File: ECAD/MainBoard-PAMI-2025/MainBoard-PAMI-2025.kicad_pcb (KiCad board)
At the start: 2 copper layers, 80 x 80 mm, 53 parts, among them J1 Sensor_Center, J10 Serial, J11 Con_Batt, J13 OLED, J2 USB_B, J3 Sensor_RIGHT, J4 Servo, J5 Sensor_LEFT, J6 Servo, J7 LeftMotor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

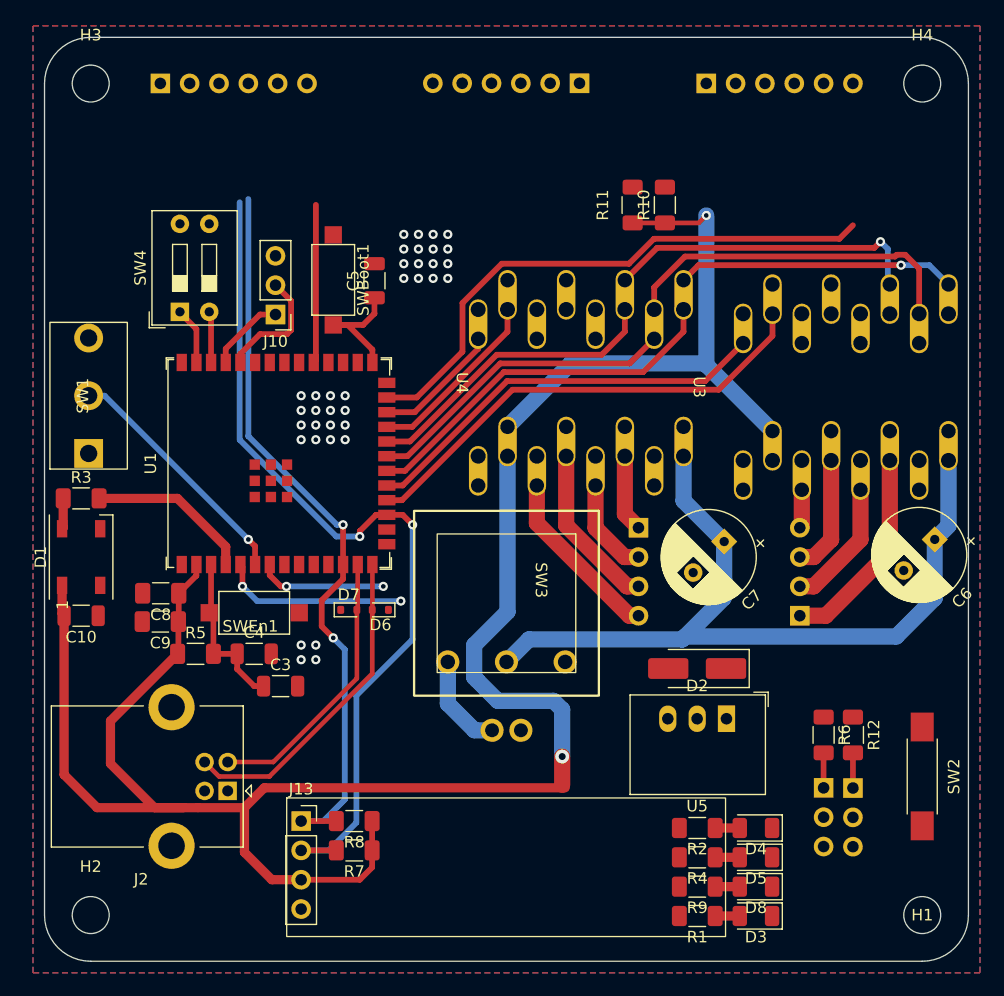
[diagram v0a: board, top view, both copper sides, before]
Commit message: Update Live 206
Update Battery
Add Recom 5V
Add ASM1117
Add capacitor
Change sensor header
Move components
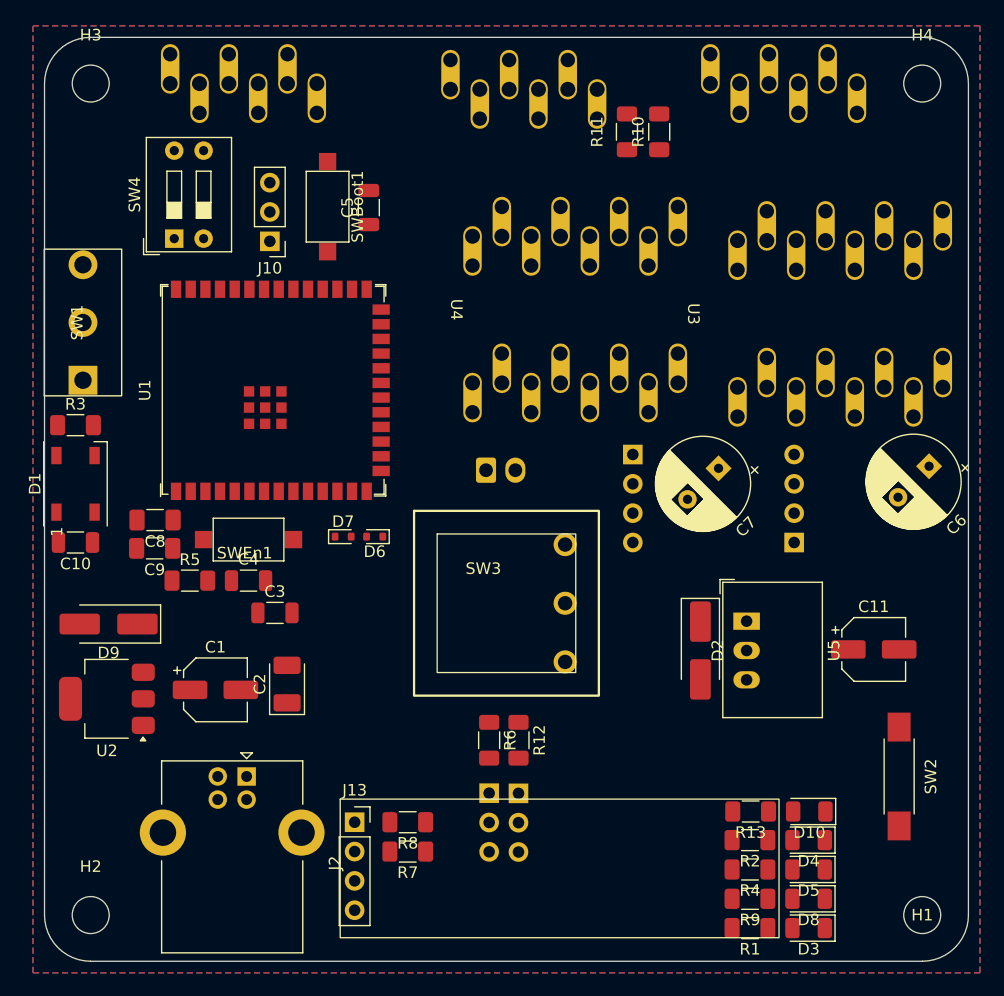
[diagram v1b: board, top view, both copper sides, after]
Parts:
- added C1: 10uF, Capacitor_SMD:CP_Elec_5x5.4, F.Cu at (94.8, 121.5)
- added C11: 22uF, Capacitor_SMD:CP_Elec_5x5.4, F.Cu at (151.8, 118.0)
- added C2: 22uF, Capacitor_Tantalum_SMD:CP_EIA-3528-12_Kemet-T_Pad1.50x2.35mm_HandSolder, F.Cu at (101.0, 121.0)
- added D10: Green, LED_SMD:LED_1206_3216Metric, F.Cu at (146.2, 132.0)
- added D9: D_Small, Diode_SMD:D_SMA_Handsoldering, F.Cu at (85.5, 115.8)
- added R13: 1K, Resistor_SMD:R_1206_3216Metric_Pad1.30x1.75mm_HandSolder, F.Cu at (141.1, 132.0)
- added U2: AMS1117-3.3, Package_TO_SOT_SMD:SOT-223-3_TabPin2, F.Cu at (85.4, 122.3)
- J1, J3, J5: footprint Connector_PinSocket_2.54mm:PinSocket_1x06_P2.54mm_Vertical -> PAMI-2025:VL53 Bottom Entry Version
- J11: footprint PAMI-2025:LP-e6 Batterie -> Connector_Molex:Molex_KK-254_AE-6410-02A_1x02_P2.54mm_Vertical
- U5: value R-78E3.3-1.0 -> R-78E5.0-1.0
- moved J4 29.0 mm to (118.5, 130.4)
- moved R6 29.0 mm to (118.5, 125.9)
- moved J6 29.0 mm to (121.0, 130.5)
- moved R12 29.0 mm to (121.0, 125.9)
- moved J11 22.6 mm to (118.2, 102.5), turned to 0 degrees
- moved U5 8.62 mm to (140.8, 115.6), turned to -90 degrees
- moved J5 7.20 mm to (97.2, 69.0)
- moved J3 6.70 mm to (144.0, 69.0)
- moved C4 6.36 mm to (97.7, 112.0)
- moved C6 6.36 mm to (156.6, 102.1)
- moved C7 6.36 mm to (138.4, 102.3)
- moved D6 6.36 mm to (108.6, 108.2)
- moved D7 6.36 mm to (105.9, 108.2)
- moved J8 6.36 mm to (144.9, 108.7)
- moved U3 6.36 mm to (148.9, 88.9)
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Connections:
- C6 pad 1: +5VP -> +9V
- C7 pad 1: +5VP -> +9V
- D2 pad 1: +5VP -> +9V
- D2 pad 2: +3.3V -> +5VP
- J4 pad 2: +3.3V -> +5VP
- J6 pad 2: +3.3V -> +5VP
- R2 pad 2: +5VP -> +9V
- SW3 pad 2: +5VP -> +9V
- U3 pad 16: +5VP -> +9V
- U4 pad 16: +5VP -> +9V
- U5 pad 1: +5VP -> +9V
- U5 pad 3: +3.3V -> +5VP
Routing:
- net +3.3V: track 193.7 -> 0.00 mm, vias 2 -> 0
- net SCL: track 77.1 -> 0.00 mm, vias 2 -> 0
- net +5VP: track 70.6 -> 0.00 mm
- net SDA: track 64.9 -> 0.00 mm, vias 2 -> 0
- net LeftMS1: track 57.8 -> 0.00 mm
- net EnDriver: track 56.8 -> 0.00 mm, vias 1 -> 0
- net LeftMS2: track 54.0 -> 0.00 mm, vias 1 -> 0
- net XSHUT_RIGHT: track 49.0 -> 0.00 mm
- net RightStep: track 41.2 -> 0.00 mm
- net RightDir: track 36.0 -> 0.00 mm
- net /D+: track 28.2 -> 0.00 mm
- net /D-: track 24.1 -> 0.00 mm
- net Color_Team: track 21.4 -> 0.00 mm, vias 1 -> 0
- net Net-(J8-Pin_1): track 18.0 -> 0.00 mm
- net Tirette: track 16.2 -> 0.00 mm, vias 2 -> 0
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
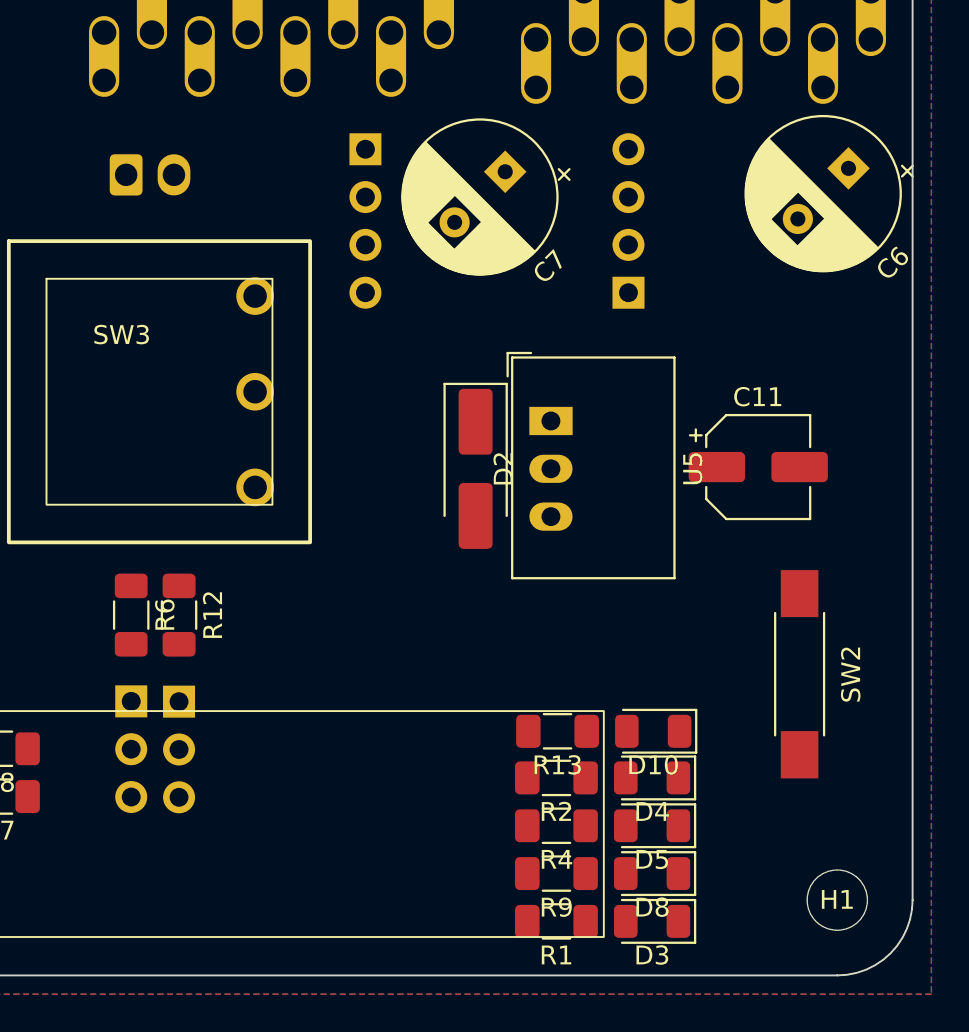
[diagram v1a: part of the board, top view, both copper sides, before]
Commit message: Add buzzer
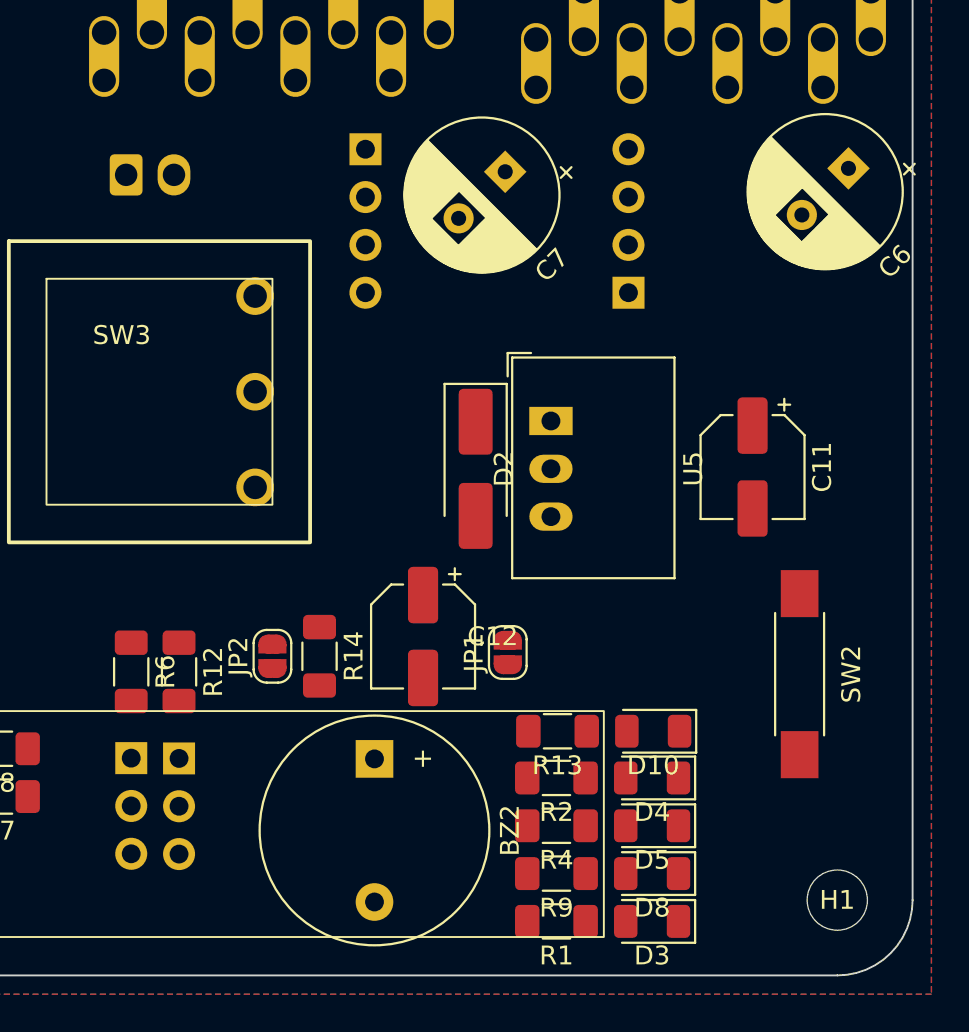
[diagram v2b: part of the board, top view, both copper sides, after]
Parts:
- added BZ2: Buzzer, Buzzer_Beeper:Buzzer_12x9.5RM7.6, F.Cu at (131.4, 133.5)
- added C12: 100uF, Capacitor_SMD:CP_Elec_5x5.4, F.Cu at (134.0, 127.0)
- added JP1: SolderJumper_2_Open, Jumper:SolderJumper-2_P1.3mm_Open_RoundedPad1.0x1.5mm, F.Cu at (138.5, 127.9)
- added JP2: SolderJumper_2_Open, Jumper:SolderJumper-2_P1.3mm_Open_RoundedPad1.0x1.5mm, F.Cu at (126.0, 128.1)
- added R14: 330, Resistor_SMD:R_1206_3216Metric_Pad1.30x1.75mm_HandSolder, F.Cu at (128.5, 128.1)
- C6, C7: footprint Capacitor_THT:CP_Radial_D8.0mm_P3.80mm -> Capacitor_THT:CP_Radial_D8.0mm_P3.50mm
- moved J4 3.02 mm to (118.5, 133.5)
- moved R12 3.02 mm to (121.0, 128.9)
- moved R6 3.02 mm to (118.5, 128.9)
- moved J6 3.01 mm to (121.0, 133.5)
- moved C11 0.30 mm to (151.5, 118.0), turned to -90 degrees
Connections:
- U1 pad 10: DAC1 -> XSHUT_CENTER
- U1 pad 11: DAC2 -> Buzzer

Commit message: routage + silkscreen
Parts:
- added G***: LOGO, LOGO, F.Cu at (115.2, 96.0)
- added G***: LOGO, LOGO, F.Cu at (106.5, 118.5)
- added G***: LOGO, LOGO, F.Cu at (143.0, 118.1)
- added G***: LOGO, LOGO, F.Cu at (137.8, 96.1)
- added G***: LOGO, LOGO, F.Cu at (123.8, 72.5)
- added G***: LOGO, LOGO, F.Cu at (115.5, 102.4)
- added G***: LOGO, LOGO, F.Cu at (106.9, 142.8)
- added G***: LOGO, LOGO, F.Cu at (138.2, 68.5)
- added G***: LOGO, LOGO, F.Cu at (104.4, 124.8)
- added G***: LOGO, LOGO, F.Cu at (116.2, 138.6)
- added G***: LOGO, LOGO, F.Cu at (99.2, 83.9)
- added G***: LOGO, LOGO, F.Cu at (94.2, 68.6)
- added kibuzzard-670C0418: G***, kibuzzard-670C0418, F.Cu at (121.0, 142.2)
- added kibuzzard-670C0436: G***, kibuzzard-670C0436, F.Cu at (118.5, 142.2)
- added kibuzzard-670C045B: G***, kibuzzard-670C045B, F.Cu at (116.0, 136.0)
- added kibuzzard-670C047F: G***, kibuzzard-670C047F, F.Cu at (123.8, 102.5)
- added kibuzzard-670C04A5: G***, kibuzzard-670C04A5, F.Cu at (135.7, 73.2)
- added kibuzzard-670C04A5: G***, kibuzzard-670C04A5, F.Cu at (126.4, 75.7)
- added kibuzzard-670C04A5: G***, kibuzzard-670C04A5, F.Cu at (109.8, 138.0)
- added kibuzzard-670C04A5: G***, kibuzzard-670C04A5, F.Cu at (91.6, 73.2)
- added kibuzzard-670C04EF: G***, kibuzzard-670C04EF, F.Cu at (106.0, 84.2)
- added kibuzzard-670C0507: G***, kibuzzard-670C0507, F.Cu at (87.5, 90.0)
- added kibuzzard-670C057C: G***, kibuzzard-670C057C, F.Cu at (92.2, 77.5)
- added kibuzzard-670C058F: G***, kibuzzard-670C058F, F.Cu at (85.5, 74.0)
- added kibuzzard-670C05E9: G***, kibuzzard-670C05E9, F.Cu at (141.5, 132.0)
- added kibuzzard-670C060B: G***, kibuzzard-670C060B, F.Cu at (149.0, 132.3)
- added kibuzzard-670C0614: G***, kibuzzard-670C0614, F.Cu at (146.5, 132.0)
- added kibuzzard-670C061D: G***, kibuzzard-670C061D, F.Cu at (144.0, 131.7)
- added kibuzzard-670C0624: G***, kibuzzard-670C0624, F.Cu at (139.0, 132.0)
- added kibuzzard-670C063A: G***, kibuzzard-670C063A, F.Cu at (156.0, 129.0)
- added kibuzzard-670C077D: G***, kibuzzard-670C077D, F.Cu at (97.9, 79.3)
- added kibuzzard-670C0798: G***, kibuzzard-670C0798, F.Cu at (96.5, 84.1)
- added kibuzzard-670C07A3: G***, kibuzzard-670C07A3, F.Cu at (93.9, 84.1)
- added kibuzzard-670C07E1: G***, kibuzzard-670C07E1, F.Cu at (112.2, 90.5)
- R14: value 330 -> 330R
- moved D10 9.47 mm to (146.5, 141.5), turned to 90 degrees
- moved R11 9.40 mm to (138.5, 78.0), turned to 0 degrees
- moved C2 8.28 mm to (93.0, 123.1), turned to -90 degrees
- moved R2 8.16 mm to (149.0, 136.5), turned to 90 degrees
- moved D4 7.54 mm to (149.0, 141.5), turned to 90 degrees
- moved D3 7.19 mm to (139.0, 141.5), turned to 90 degrees
- moved R13 6.98 mm to (146.5, 136.5), turned to 90 degrees
- moved D5 6.45 mm to (141.5, 141.5), turned to 90 degrees
- moved R1 6.00 mm to (139.0, 136.5), turned to 90 degrees
- moved R10 5.76 mm to (138.5, 75.5), turned to 0 degrees
- moved J10 5.63 mm to (94.0, 81.5), turned to 90 degrees
- moved R9 4.25 mm to (144.0, 136.5), turned to 90 degrees
- moved C1 3.35 mm to (98.0, 120.5), turned to -90 degrees
- moved SW4 3.30 mm to (89.3, 79.8), turned to 180 degrees
- moved D8 2.89 mm to (144.0, 141.5), turned to 90 degrees
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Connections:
- J1 pad 5: GPIOI_CENTER -> unconnected-(J1-Pin_5-Pad5)
- J3 pad 5: GPIOI_RIGHT -> unconnected-(J3-Pin_5-Pad5)
- J5 pad 5: GPIOI_LEFT -> unconnected-(J5-Pin_5-Pad5)
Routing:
- net +3.3V: track 0.00 -> 283.0 mm, vias 0 -> 2
- net +9V: track 0.00 -> 151.2 mm, vias 0 -> 1
- net SCL: track 0.00 -> 134.5 mm, vias 0 -> 4
- net SDA: track 0.00 -> 127.9 mm, vias 0 -> 2
- net Tirette: track 0.00 -> 78.3 mm, vias 0 -> 2
- net Net-(J2-VBUS): track 0.00 -> 60.0 mm, vias 0 -> 1
- net EnDriver: track 0.00 -> 58.2 mm
- net LeftMS1: track 0.00 -> 58.2 mm, vias 0 -> 1
- net LeftMS2: track 0.00 -> 53.8 mm, vias 0 -> 1
- net +5VP: track 0.00 -> 51.1 mm
- net XSHUT_RIGHT: track 0.00 -> 48.6 mm, vias 0 -> 1
- net +BATT: track 0.00 -> 46.9 mm
- net Buzzer: track 0.00 -> 45.2 mm, vias 0 -> 2
- net RightStep: track 0.00 -> 42.3 mm
- net XSHUT_CENTER: track 0.00 -> 38.3 mm, vias 0 -> 2
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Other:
- board text added: "Barbatronic"
- board text added: "Karibous 2024-25"

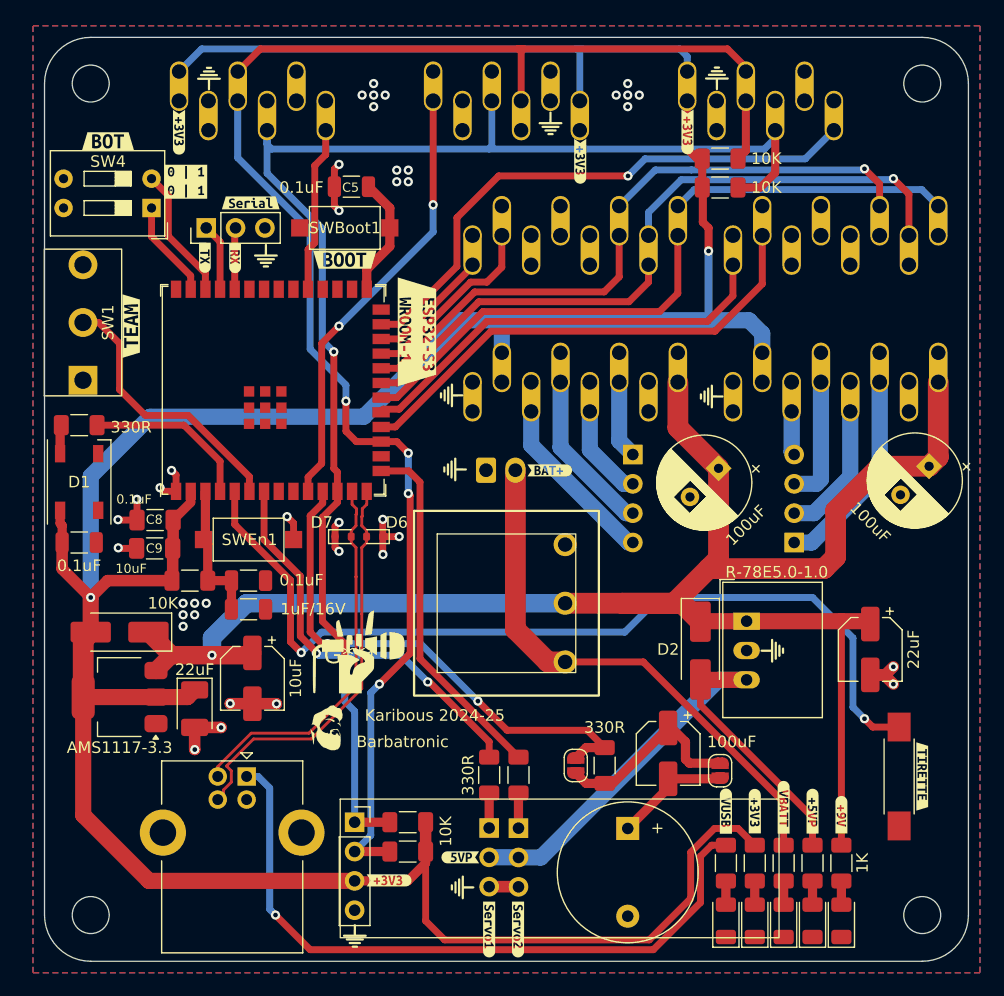
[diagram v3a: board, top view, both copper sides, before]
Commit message: Change for DRV5023 - New 3D
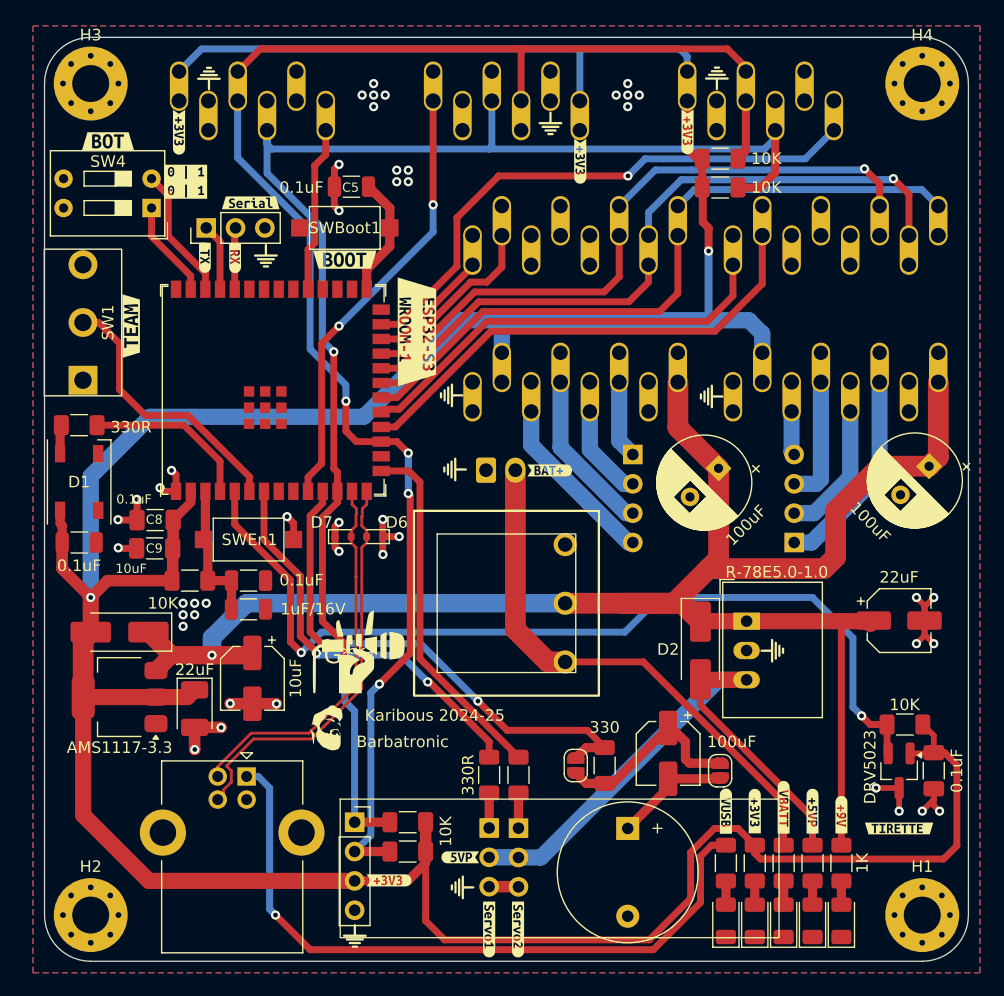
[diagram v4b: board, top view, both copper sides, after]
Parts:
- removed SW2: SW_Reed, Button_Switch_SMD:SW_SPST_REED_CT05-XXXX-G1
- removed kibuzzard-670C063A: G***, kibuzzard-670C063A
- added C13: 0.1uF, Capacitor_SMD:C_1206_3216Metric_Pad1.33x1.80mm_HandSolder, F.Cu at (157.0, 128.5)
- added R15: 10K, Resistor_SMD:R_1206_3216Metric_Pad1.30x1.75mm_HandSolder, F.Cu at (154.5, 124.5)
- added U6: DRV5023, Package_TO_SOT_SMD:SOT-23_Handsoldering, F.Cu at (154.0, 128.5)
- added kibuzzard-670C23C9: G***, kibuzzard-670C23C9, F.Cu at (154.0, 133.5)
- H1, H2, H3, H4: footprint MountingHole:MountingHole_3.2mm_M3 -> MountingHole:MountingHole_3.2mm_M3_Pad_Via
- R14: value 330R -> 330
- moved C11 3.54 mm to (154.0, 115.5), turned to 0 degrees
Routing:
- net +3.3V: track 283.0 -> 316.3 mm
- net GND: track 37.8 -> 50.9 mm, vias 39 -> 45
- net Tirette: track 78.3 -> 79.7 mm
